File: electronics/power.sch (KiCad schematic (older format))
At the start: 64 parts, among them Q1 2N7002, Q2 2N7002, SW2 PushButton, U10 INA213-SC70, U11 LT1965, U12 MCP73831, U13 DRV8839, U14 DRV8839, U7 LT1965, U8 LT1965, U9 LTC2955DDB-1

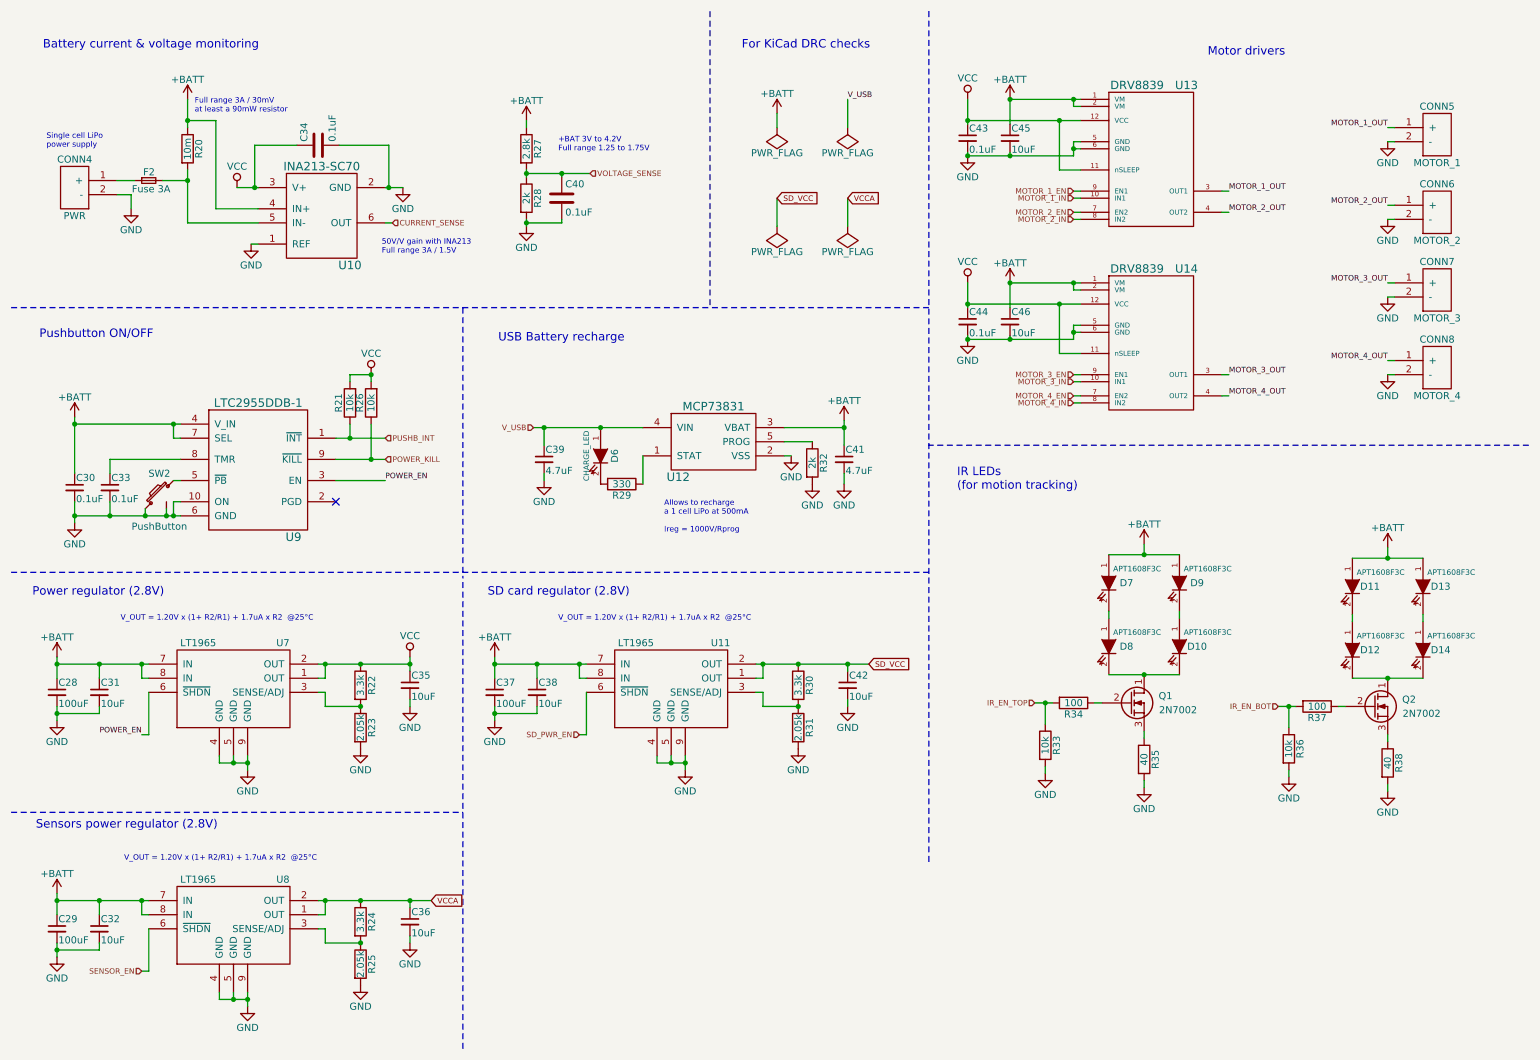
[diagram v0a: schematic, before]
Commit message: Use wifi for telemetry
Cleanup schematic
Use ESP12E (wifi) for telemetry instead of NRF24
Reannotate & replot pdf
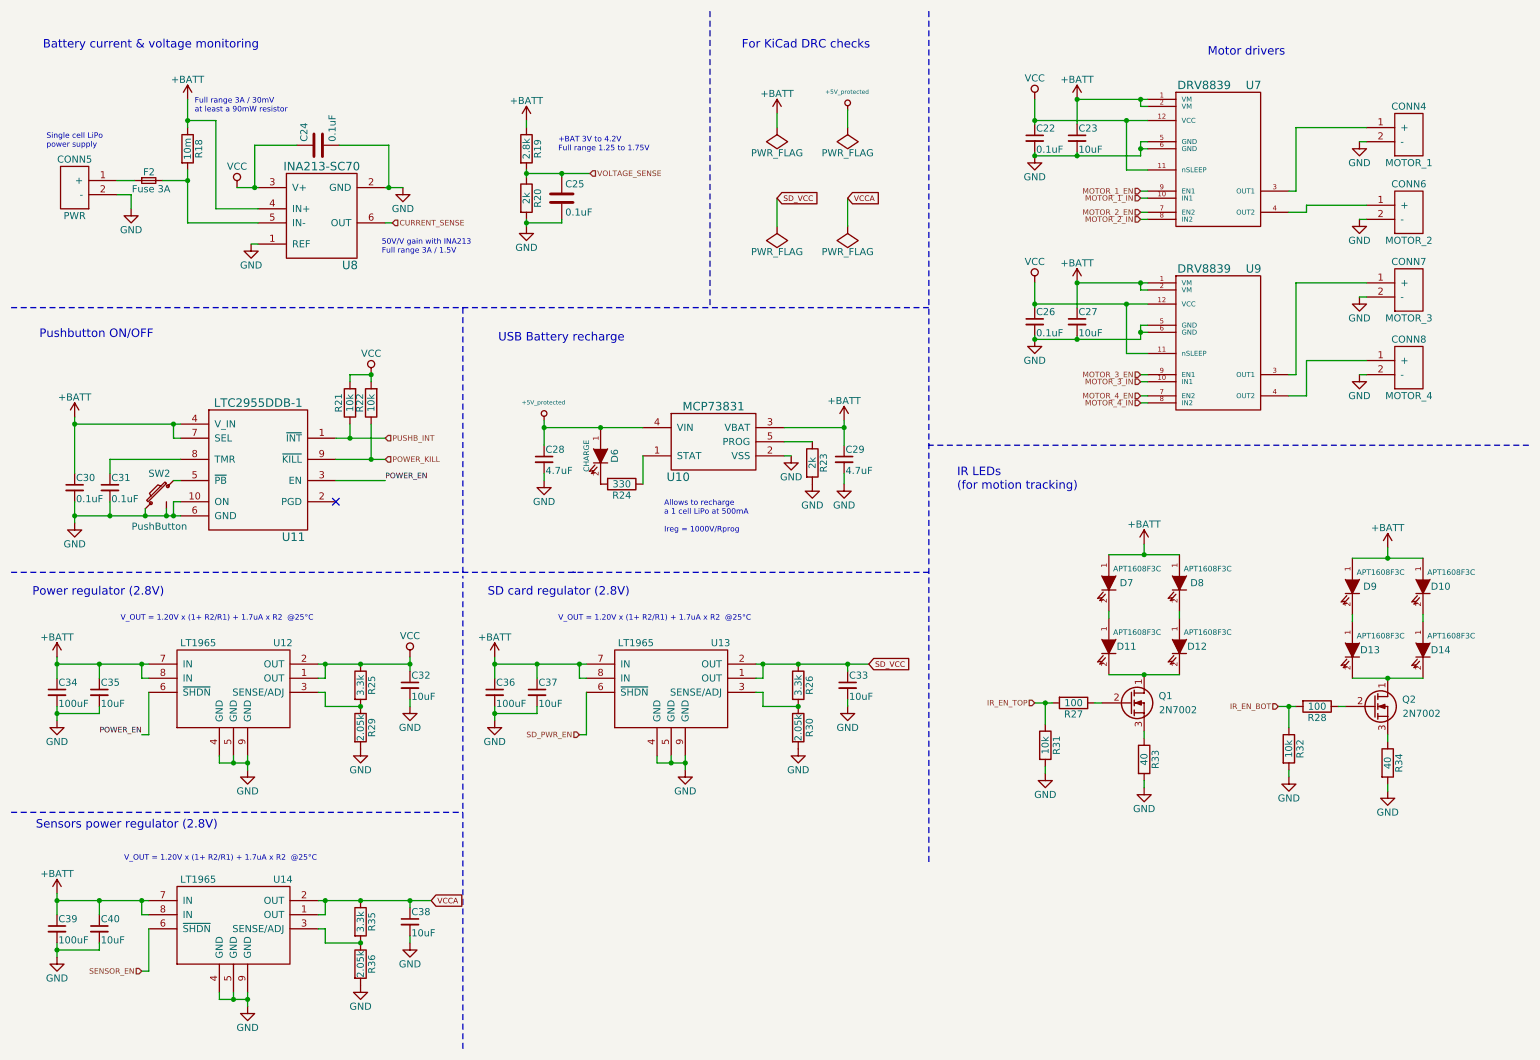
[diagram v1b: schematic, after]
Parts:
- D6: value CHARGE_LED -> CHARGE
- renumbered C43 to C22, C45 to C23, C34 to C24, C40 to C25, C44 to C26, C46 to C27, C39 to C28, C41 to C29, C33 to C31, C35 to C32, C42 to C33, C28 to C34, C31 to C35, C37 to C36, C38 to C37, C36 to C38, C29 to C39, C32 to C40, CONN5 to CONN4, CONN4 to CONN5, D13 to D10, D8 to D11, D10 to D12, D12 to D13, D9 to D8, D11 to D9, R20 to R18, R27 to R19, R28 to R20, R26 to R22, R32 to R23, R29 to R24, R22 to R25, R30 to R26, R34 to R27, R37 to R28, R23 to R29, R31 to R30, R33 to R31, R36 to R32, R35 to R33, R38 to R34, R24 to R35, R25 to R36, U12 to U10, U9 to U11, U7 to U12, U11 to U13, U8 to U14, U13 to U7, U10 to U8, U14 to U9
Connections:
- net MOTOR_1_OUT: no longer names the net of CONN4.1 (+), U7.3 (OUT1)
- net MOTOR_2_OUT: no longer names the net of CONN6.1 (+), U7.4 (OUT2)
- net MOTOR_3_OUT: no longer names the net of CONN7.1 (+), U9.3 (OUT1)
- net MOTOR_4_OUT: no longer names the net of CONN8.1 (+), U9.4 (OUT2)
- net V_USB renamed +5V_protected
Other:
- moved on the sheet: C22, C23, C26, C27, CONN4, CONN6, CONN7, CONN8, U7, U9

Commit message: Finish routing
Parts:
- C23, C27, C32, C33, C34, C35, C36, C37, C38, C39, C40: footprint _std:_0603 -> _std:C_0603
- D10, D11, D12, D13, D14, D6, D7, D8, D9: footprint _std:_LED_0603 -> _std:D_0603
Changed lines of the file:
@@
 F 0 "D6" H 4650 3725 50  0000 C CNN
 F 1 "CHARGE" H 4650 3525 39  0000 C CNN
-F 2 "_std:_LED_0603" H 4650 3625 60  0001 C CNN
+F 2 "_std:D_0603" H 4650 3625 60  0001 C CNN
 F 3 "" H 4650 3625 60  0000 C CNN
 	1    4650 3625
@@
 F 0 "C32" H 3310 5320 50  0000 L CNN
 F 1 "10uF" H 3310 5170 50  0000 L CNN
-F 2 "_std:_0603" H 3300 5250 60  0001 C CNN
+F 2 "_std:C_0603" H 3300 5250 60  0001 C CNN
 F 3 "" H 3300 5250 60  0000 C CNN
 	1    3300 5250
@@
 F 0 "C35" H 1110 5370 50  0000 L CNN
 F 1 "10uF" H 1110 5220 50  0000 L CNN
-F 2 "_std:_0603" H 1100 5300 60  0001 C CNN
+F 2 "_std:C_0603" H 1100 5300 60  0001 C CNN
 F 3 "" H 1100 5300 60  0000 C CNN
 	1    1100 5300
@@
 F 0 "C34" H 810 5370 50  0000 L CNN
 F 1 "100uF" H 810 5220 50  0000 L CNN
-F 2 "_std:_0603" H 800 5300 60  0001 C CNN
+F 2 "_std:C_0603" H 800 5300 60  0001 C CNN
 F 3 "" H 800 5300 60  0000 C CNN
 	1    800  5300
@@
 F 0 "C27" H 8035 2745 50  0000 L CNN
 F 1 "10uF" H 8035 2595 50  0000 L CNN
-F 2 "_std:_0603" H 8025 2675 60  0001 C CNN
+F 2 "_std:C_0603" H 8025 2675 60  0001 C CNN
 F 3 "" H 8025 2675 60  0000 C CNN
 	1    8025 2675
@@
 F 0 "C23" H 8035 1445 50  0000 L CNN
 F 1 "10uF" H 8035 1295 50  0000 L CNN
-F 2 "_std:_0603" H 8025 1375 60  0001 C CNN
+F 2 "_std:C_0603" H 8025 1375 60  0001 C CNN
 F 3 "" H 8025 1375 60  0000 C CNN
 	1    8025 1375
@@
 F 0 "D7" V 8250 4650 50  0000 C CNN
 F 1 "APT1608F3C" V 8150 4725 39  0000 C CNN
-F 2 "_std:_LED_0603" H 8250 4525 60  0001 C CNN
+F 2 "_std:D_0603" H 8250 4525 60  0001 C CNN
 F 3 "" H 8250 4525 60  0000 C CNN
 	1    8250 4525
@@
 F 0 "D11" V 8250 5100 50  0000 C CNN
 F 1 "APT1608F3C" V 8150 5175 39  0000 C CNN
-F 2 "_std:_LED_0603" H 8250 4975 60  0001 C CNN
+F 2 "_std:D_0603" H 8250 4975 60  0001 C CNN
 F 3 "" H 8250 4975 60  0000 C CNN
 	1    8250 4975
@@
 F 0 "D12" V 8750 5100 50  0000 C CNN
 F 1 "APT1608F3C" V 8650 5175 39  0000 C CNN
-F 2 "_std:_LED_0603" H 8750 4975 60  0001 C CNN
+F 2 "_std:D_0603" H 8750 4975 60  0001 C CNN
 F 3 "" H 8750 4975 60  0000 C CNN
 	1    8750 4975
@@
 F 0 "D8" V 8750 4650 50  0000 C CNN
 F 1 "APT1608F3C" V 8650 4725 39  0000 C CNN
-F 2 "_std:_LED_0603" H 8750 4525 60  0001 C CNN
+F 2 "_std:D_0603" H 8750 4525 60  0001 C CNN
 F 3 "" H 8750 4525 60  0000 C CNN
 	1    8750 4525
@@
 F 0 "D9" V 9975 4675 50  0000 C CNN
 F 1 "APT1608F3C" V 9875 4750 39  0000 C CNN
-F 2 "_std:_LED_0603" H 9975 4550 60  0001 C CNN
+F 2 "_std:D_0603" H 9975 4550 60  0001 C CNN
 F 3 "" H 9975 4550 60  0000 C CNN
 	1    9975 4550
@@
 F 0 "D13" V 9975 5125 50  0000 C CNN
 F 1 "APT1608F3C" V 9875 5200 39  0000 C CNN
-F 2 "_std:_LED_0603" H 9975 5000 60  0001 C CNN
+F 2 "_std:D_0603" H 9975 5000 60  0001 C CNN
 F 3 "" H 9975 5000 60  0000 C CNN
 	1    9975 5000
@@
 F 0 "D14" V 10475 5125 50  0000 C CNN
 F 1 "APT1608F3C" V 10375 5200 39  0000 C CNN
-F 2 "_std:_LED_0603" H 10475 5000 60  0001 C CNN
+F 2 "_std:D_0603" H 10475 5000 60  0001 C CNN
 F 3 "" H 10475 5000 60  0000 C CNN
 	1    10475 5000
@@
 F 0 "D10" V 10475 4675 50  0000 C CNN
 F 1 "APT1608F3C" V 10375 4750 39  0000 C CNN
-F 2 "_std:_LED_0603" H 10475 4550 60  0001 C CNN
+F 2 "_std:D_0603" H 10475 4550 60  0001 C CNN
 F 3 "" H 10475 4550 60  0000 C CNN
 	1    10475 4550
@@
 F 0 "C38" H 3310 6995 50  0000 L CNN
 F 1 "10uF" H 3310 6845 50  0000 L CNN
-F 2 "_std:_0603" H 3300 6925 60  0001 C CNN
+F 2 "_std:C_0603" H 3300 6925 60  0001 C CNN
 F 3 "" H 3300 6925 60  0000 C CNN
 	1    3300 6925
@@
 F 0 "C40" H 1110 7045 50  0000 L CNN
 F 1 "10uF" H 1110 6895 50  0000 L CNN
-F 2 "_std:_0603" H 1100 6975 60  0001 C CNN
+F 2 "_std:C_0603" H 1100 6975 60  0001 C CNN
 F 3 "" H 1100 6975 60  0000 C CNN
 	1    1100 6975
@@
 F 0 "C39" H 810 7045 50  0000 L CNN
 F 1 "100uF" H 810 6895 50  0000 L CNN
-F 2 "_std:_0603" H 800 6975 60  0001 C CNN
+F 2 "_std:C_0603" H 800 6975 60  0001 C CNN
 F 3 "" H 800 6975 60  0000 C CNN
 	1    800  6975
@@
 F 0 "C33" H 6410 5320 50  0000 L CNN
 F 1 "10uF" H 6410 5170 50  0000 L CNN
-F 2 "_std:_0603" H 6400 5250 60  0001 C CNN
+F 2 "_std:C_0603" H 6400 5250 60  0001 C CNN
 F 3 "" H 6400 5250 60  0000 C CNN
 	1    6400 5250
@@
 F 0 "C37" H 4210 5370 50  0000 L CNN
 F 1 "10uF" H 4210 5220 50  0000 L CNN
-F 2 "_std:_0603" H 4200 5300 60  0001 C CNN
+F 2 "_std:C_0603" H 4200 5300 60  0001 C CNN
 F 3 "" H 4200 5300 60  0000 C CNN
 	1    4200 5300
@@
 F 0 "C36" H 3910 5370 50  0000 L CNN
 F 1 "100uF" H 3910 5220 50  0000 L CNN
-F 2 "_std:_0603" H 3900 5300 60  0001 C CNN
+F 2 "_std:C_0603" H 3900 5300 60  0001 C CNN
 F 3 "" H 3900 5300 60  0000 C CNN
 	1    3900 5300
